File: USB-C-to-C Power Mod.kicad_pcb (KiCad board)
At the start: 2 copper layers, 7.8 x 4.5 mm, 6 parts, among them J1 CC1, J2 CC2

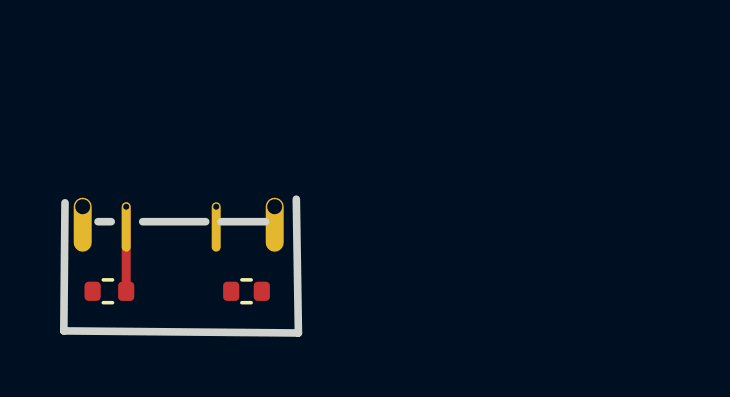
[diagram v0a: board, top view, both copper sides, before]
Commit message: First version of board with complete edge cuts
This is the first complete version of the board with the edge cuts, traces, and pads.
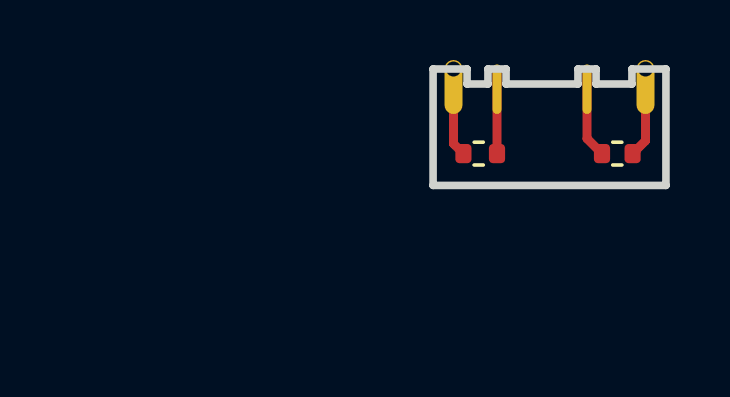
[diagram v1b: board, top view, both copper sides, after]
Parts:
- moved J1 13.2 mm to (146.9, 92.9)
- moved J2 13.2 mm to (140.7, 92.9)
- moved GND 13.2 mm to (143.7, 88.8)
- moved GND 13.2 mm to (151.1, 88.6)
- moved R1 13.2 mm to (147.2, 92.7)
- moved R2 13.2 mm to (142.6, 92.7)
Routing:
- net GND: track 0.00 -> 5.95 mm
- net Net-(J1-Pad1): track 0.00 -> 3.03 mm
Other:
- board size 7.8 x 4.5 mm -> 7.8 x 3.9 mm
- board text added: "USB C2C [ide]"
- board text removed: "C-to-C mod by ide"

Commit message: Adjust edge cuts to give fingers more clearance + duplicate PCB for OSH Park
The tolerances of the edge cuts are somewhat large (+/- 5 mil) so nudge the edge cuts up by 5 mil. If needed, it's easy to trim the flex PCB if the fingers are too long.

Also, the PCB is too small for OSH Park so duplicate it to meet their minimum size.
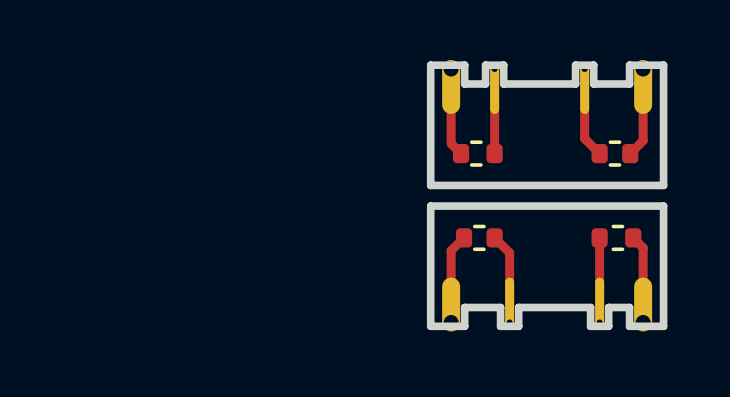
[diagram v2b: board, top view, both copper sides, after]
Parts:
- added GND: GND, FlexPCB:Plated_Hole_D0.6mm, F.Cu at (146.1, 99.5)
- added GND: GND, FlexPCB:Plated_Hole_D0.6mm, F.Cu at (138.8, 99.7)
- added J1: CC1, FlexPCB:Plated_Hole_D0.3mm, F.Cu at (142.9, 95.4)
- added J2: CC2, FlexPCB:Plated_Hole_D0.3mm, F.Cu at (149.2, 95.4)
- added R1: 5.1K, Resistor_SMD:R_0402_1005Metric, F.Cu at (142.6, 95.5)
- added R2: 5.1K, Resistor_SMD:R_0402_1005Metric, F.Cu at (147.2, 95.5)
- moved J1 0.08 mm to (146.8, 92.9)
- moved J2 0.08 mm to (140.6, 92.9)
- moved R1 0.08 mm to (147.1, 92.7)
- moved R2 0.08 mm to (142.5, 92.7)
- moved GND 0.08 mm to (143.7, 88.8)
- moved GND 0.08 mm to (151.0, 88.6)
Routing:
- net GND: track 5.95 -> 11.9 mm
- net Net-(J1-Pad1): track 3.03 -> 6.05 mm
- net Net-(J2-Pad1): track 2.82 -> 5.64 mm
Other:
- board size 7.8 x 3.9 mm -> 7.8 x 8.7 mm
